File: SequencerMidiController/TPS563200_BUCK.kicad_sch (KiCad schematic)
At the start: 13 parts, among them U38 TPS563200

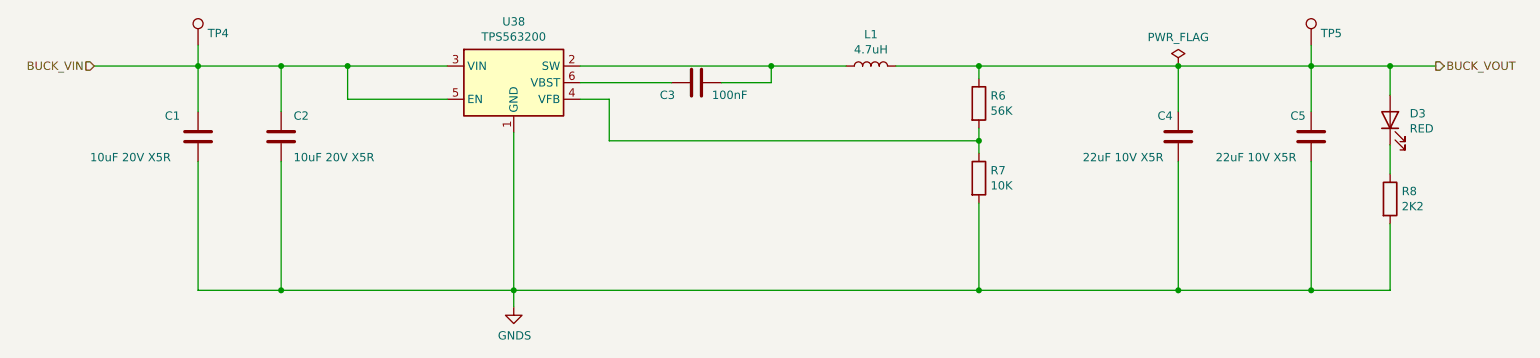
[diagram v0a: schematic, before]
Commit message: updated SPI labels
https://github.com/cracked-machine/BassStationSequencerMidiController/issues/3
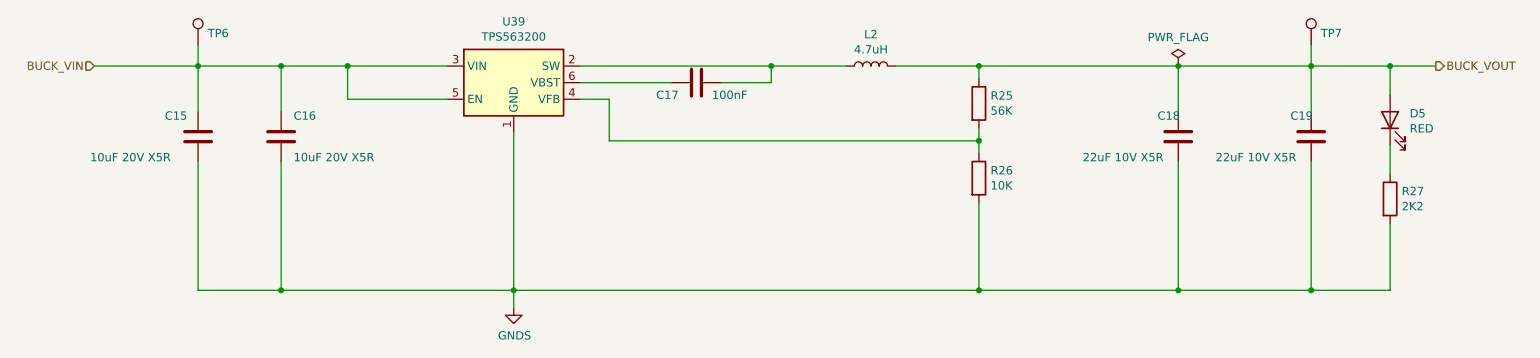
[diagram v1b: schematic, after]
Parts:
- renumbered C1 to C15, C2 to C16, C3 to C17, C4 to C18, C5 to C19, D3 to D5, L1 to L2, R6 to R25, R7 to R26, R8 to R27, TP4 to TP6, TP5 to TP7, U38 to U39
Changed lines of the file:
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@@
   (symbol (lib_id "Regulator_Switching:TPS563200") (at 105.41 83.82 0)
     (in_bom yes) (on_board yes)
-    (property "Reference" "U38" (id 0) (at 105.41 74.4982 0))
+    (property "Reference" "U39" (id 0) (at 105.41 74.4982 0))
     (property "Value" "TPS563200" (id 1) (at 105.41 76.8096 0))
     (property "Footprint" "Package_TO_SOT_SMD:SOT-23-6" (id 2) (at 106.68 90.17 0)
@@
   (symbol (lib_id "power:GNDS") (at 105.41 118.11 0)
     (in_bom yes) (on_board yes)
-    (property "Reference" "#PWR0108" (id 0) (at 105.41 124.46 0)
+    (property "Reference" "#PWR023" (id 0) (at 105.41 124.46 0)
       (effects (font (size 1.27 1.27)) hide)
     )
@@
   (symbol (lib_id "Device:C") (at 57.15 92.075 0)
     (in_bom yes) (on_board yes)
-    (property "Reference" "C1" (id 0) (at 52.07 88.9 0)
+    (property "Reference" "C15" (id 0) (at 52.07 88.9 0)
       (effects (font (size 1.27 1.27)) (justify left))
     )
@@
   (symbol (lib_id "Device:C") (at 69.85 92.075 0)
     (in_bom yes) (on_board yes)
-    (property "Reference" "C2" (id 0) (at 71.755 88.9 0)
+    (property "Reference" "C16" (id 0) (at 71.755 88.9 0)
       (effects (font (size 1.27 1.27)) (justify left))
     )
@@
   (symbol (lib_id "Device:L") (at 160.02 81.28 90)
     (in_bom yes) (on_board yes)
-    (property "Reference" "L1" (id 0) (at 160.02 76.454 90))
+    (property "Reference" "L2" (id 0) (at 160.02 76.454 90))
     (property "Value" "4.7uH" (id 1) (at 160.02 78.7654 90))
     (property "Footprint" "Inductor_SMD:L_Taiyo-Yuden_NR-80xx_HandSoldering" (id 2) (at 160.02 81.28 0)
@@
   (symbol (lib_id "Device:C") (at 133.35 83.82 90)
     (in_bom yes) (on_board yes)
-    (property "Reference" "C3" (id 0) (at 128.905 85.725 90))
+    (property "Reference" "C17" (id 0) (at 128.905 85.725 90))
     (property "Value" "100nF" (id 1) (at 138.43 85.725 90))
     (property "Footprint" "Capacitor_SMD:C_0805_2012Metric_Pad1.18x1.45mm_HandSolder" (id 2) (at 137.16 82.8548 0)
@@
   (symbol (lib_id "Device:R") (at 176.53 86.995 0)
     (in_bom yes) (on_board yes)
-    (property "Reference" "R6" (id 0) (at 178.308 85.8266 0)
+    (property "Reference" "R25" (id 0) (at 178.308 85.8266 0)
       (effects (font (size 1.27 1.27)) (justify left))
     )
@@
   (symbol (lib_id "Device:R") (at 176.53 98.425 0)
     (in_bom yes) (on_board yes)
-    (property "Reference" "R7" (id 0) (at 178.308 97.2566 0)
+    (property "Reference" "R26" (id 0) (at 178.308 97.2566 0)
       (effects (font (size 1.27 1.27)) (justify left))
     )
@@
   (symbol (lib_id "Device:C") (at 207.01 92.075 0)
     (in_bom yes) (on_board yes)
-    (property "Reference" "C4" (id 0) (at 203.835 88.9 0)
+    (property "Reference" "C18" (id 0) (at 203.835 88.9 0)
       (effects (font (size 1.27 1.27)) (justify left))
     )
@@
   (symbol (lib_id "Device:C") (at 227.33 92.075 0)
     (in_bom yes) (on_board yes)
-    (property "Reference" "C5" (id 0) (at 224.155 88.9 0)
+    (property "Reference" "C19" (id 0) (at 224.155 88.9 0)
       (effects (font (size 1.27 1.27)) (justify left))
     )
@@
   (symbol (lib_id "Connector:TestPoint") (at 227.33 78.105 0)
     (in_bom yes) (on_board yes)
-    (property "Reference" "TP5" (id 0) (at 228.8032 76.2762 0)
+    (property "Reference" "TP7" (id 0) (at 228.8032 76.2762 0)
       (effects (font (size 1.27 1.27)) (justify left))
     )
@@
   (symbol (lib_id "Connector:TestPoint") (at 57.15 78.105 0)
     (in_bom yes) (on_board yes)
-    (property "Reference" "TP4" (id 0) (at 58.6232 76.2762 0)
+    (property "Reference" "TP6" (id 0) (at 58.6232 76.2762 0)
       (effects (font (size 1.27 1.27)) (justify left))
     )
@@
   (symbol (lib_id "Device:LED") (at 239.395 89.535 90)
     (in_bom yes) (on_board yes)
-    (property "Reference" "D3" (id 0) (at 242.3922 88.5444 90)
+    (property "Reference" "D5" (id 0) (at 242.3922 88.5444 90)
       (effects (font (size 1.27 1.27)) (justify right))
     )
@@
   (symbol (lib_id "Device:R") (at 239.395 101.6 0)
     (in_bom yes) (on_board yes)
-    (property "Reference" "R8" (id 0) (at 241.173 100.4316 0)
+    (property "Reference" "R27" (id 0) (at 241.173 100.4316 0)
       (effects (font (size 1.27 1.27)) (justify left))
     )
@@
   (symbol (lib_id "power:PWR_FLAG") (at 207.01 81.28 0)
     (in_bom yes) (on_board yes)
-    (property "Reference" "#FLG0103" (id 0) (at 207.01 79.375 0)
-      (effects (font (size 1.27 1.27)) hide)
-    )
+    (property "Reference" "#FLG0104" (id 0) (at 207.01 79.375 0)
+      (effects (font (size 1.27 1.27)) hide)
+    )

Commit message: updated user buttons
removed dipsw, added four more tactile button (three above display, three below display, six total)
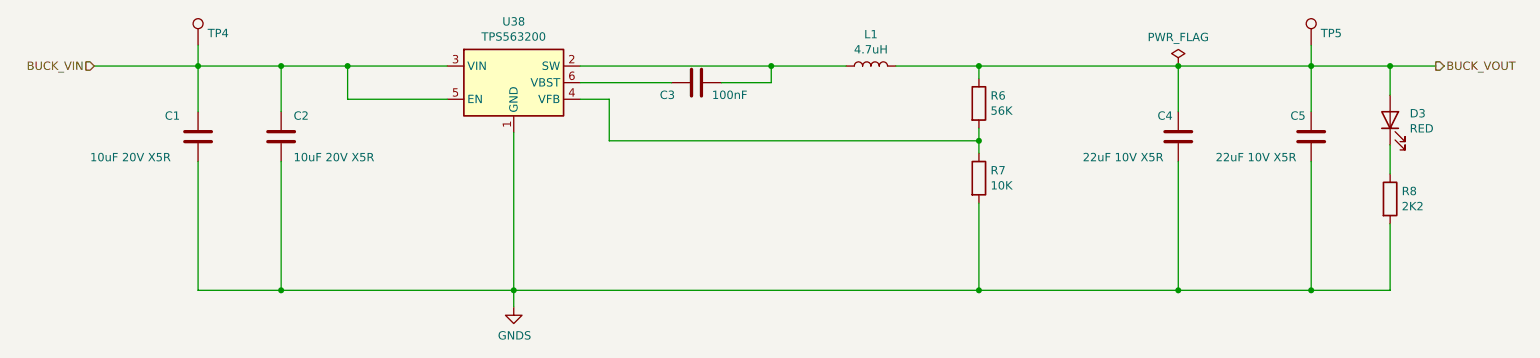
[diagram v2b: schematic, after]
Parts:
- renumbered C15 to C1, C16 to C2, C17 to C3, C18 to C4, C19 to C5, D5 to D3, L2 to L1, R25 to R6, R26 to R7, R27 to R8, TP6 to TP4, TP7 to TP5, U39 to U38
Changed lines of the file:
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@@
   (symbol (lib_id "Regulator_Switching:TPS563200") (at 105.41 83.82 0)
     (in_bom yes) (on_board yes)
-    (property "Reference" "U39" (id 0) (at 105.41 74.4982 0))
+    (property "Reference" "U38" (id 0) (at 105.41 74.4982 0))
     (property "Value" "TPS563200" (id 1) (at 105.41 76.8096 0))
     (property "Footprint" "Package_TO_SOT_SMD:SOT-23-6" (id 2) (at 106.68 90.17 0)
@@
   (symbol (lib_id "power:GNDS") (at 105.41 118.11 0)
     (in_bom yes) (on_board yes)
-    (property "Reference" "#PWR023" (id 0) (at 105.41 124.46 0)
+    (property "Reference" "#PWR0108" (id 0) (at 105.41 124.46 0)
       (effects (font (size 1.27 1.27)) hide)
     )
@@
   (symbol (lib_id "Device:C") (at 57.15 92.075 0)
     (in_bom yes) (on_board yes)
-    (property "Reference" "C15" (id 0) (at 52.07 88.9 0)
+    (property "Reference" "C1" (id 0) (at 52.07 88.9 0)
       (effects (font (size 1.27 1.27)) (justify left))
     )
@@
   (symbol (lib_id "Device:C") (at 69.85 92.075 0)
     (in_bom yes) (on_board yes)
-    (property "Reference" "C16" (id 0) (at 71.755 88.9 0)
+    (property "Reference" "C2" (id 0) (at 71.755 88.9 0)
       (effects (font (size 1.27 1.27)) (justify left))
     )
@@
   (symbol (lib_id "Device:L") (at 160.02 81.28 90)
     (in_bom yes) (on_board yes)
-    (property "Reference" "L2" (id 0) (at 160.02 76.454 90))
+    (property "Reference" "L1" (id 0) (at 160.02 76.454 90))
     (property "Value" "4.7uH" (id 1) (at 160.02 78.7654 90))
     (property "Footprint" "Inductor_SMD:L_Taiyo-Yuden_NR-80xx_HandSoldering" (id 2) (at 160.02 81.28 0)
@@
   (symbol (lib_id "Device:C") (at 133.35 83.82 90)
     (in_bom yes) (on_board yes)
-    (property "Reference" "C17" (id 0) (at 128.905 85.725 90))
+    (property "Reference" "C3" (id 0) (at 128.905 85.725 90))
     (property "Value" "100nF" (id 1) (at 138.43 85.725 90))
     (property "Footprint" "Capacitor_SMD:C_0805_2012Metric_Pad1.18x1.45mm_HandSolder" (id 2) (at 137.16 82.8548 0)
@@
   (symbol (lib_id "Device:R") (at 176.53 86.995 0)
     (in_bom yes) (on_board yes)
-    (property "Reference" "R25" (id 0) (at 178.308 85.8266 0)
+    (property "Reference" "R6" (id 0) (at 178.308 85.8266 0)
       (effects (font (size 1.27 1.27)) (justify left))
     )
@@
   (symbol (lib_id "Device:R") (at 176.53 98.425 0)
     (in_bom yes) (on_board yes)
-    (property "Reference" "R26" (id 0) (at 178.308 97.2566 0)
+    (property "Reference" "R7" (id 0) (at 178.308 97.2566 0)
       (effects (font (size 1.27 1.27)) (justify left))
     )
@@
   (symbol (lib_id "Device:C") (at 207.01 92.075 0)
     (in_bom yes) (on_board yes)
-    (property "Reference" "C18" (id 0) (at 203.835 88.9 0)
+    (property "Reference" "C4" (id 0) (at 203.835 88.9 0)
       (effects (font (size 1.27 1.27)) (justify left))
     )
@@
   (symbol (lib_id "Device:C") (at 227.33 92.075 0)
     (in_bom yes) (on_board yes)
-    (property "Reference" "C19" (id 0) (at 224.155 88.9 0)
+    (property "Reference" "C5" (id 0) (at 224.155 88.9 0)
       (effects (font (size 1.27 1.27)) (justify left))
     )
@@
   (symbol (lib_id "Connector:TestPoint") (at 227.33 78.105 0)
     (in_bom yes) (on_board yes)
-    (property "Reference" "TP7" (id 0) (at 228.8032 76.2762 0)
+    (property "Reference" "TP5" (id 0) (at 228.8032 76.2762 0)
       (effects (font (size 1.27 1.27)) (justify left))
     )
@@
   (symbol (lib_id "Connector:TestPoint") (at 57.15 78.105 0)
     (in_bom yes) (on_board yes)
-    (property "Reference" "TP6" (id 0) (at 58.6232 76.2762 0)
+    (property "Reference" "TP4" (id 0) (at 58.6232 76.2762 0)
       (effects (font (size 1.27 1.27)) (justify left))
     )
@@
   (symbol (lib_id "Device:LED") (at 239.395 89.535 90)
     (in_bom yes) (on_board yes)
-    (property "Reference" "D5" (id 0) (at 242.3922 88.5444 90)
+    (property "Reference" "D3" (id 0) (at 242.3922 88.5444 90)
       (effects (font (size 1.27 1.27)) (justify right))
     )
@@
   (symbol (lib_id "Device:R") (at 239.395 101.6 0)
     (in_bom yes) (on_board yes)
-    (property "Reference" "R27" (id 0) (at 241.173 100.4316 0)
+    (property "Reference" "R8" (id 0) (at 241.173 100.4316 0)
       (effects (font (size 1.27 1.27)) (justify left))
     )
@@
   (symbol (lib_id "power:PWR_FLAG") (at 207.01 81.28 0)
     (in_bom yes) (on_board yes)
-    (property "Reference" "#FLG0104" (id 0) (at 207.01 79.375 0)
-      (effects (font (size 1.27 1.27)) hide)
-    )
+    (property "Reference" "#FLG0103" (id 0) (at 207.01 79.375 0)
+      (effects (font (size 1.27 1.27)) hide)
+    )
